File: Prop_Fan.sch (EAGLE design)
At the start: 120 parts, among them J1 1546215-2, J2 1546215-2, J3 1546215-2, J4 1546215-2, SW2 EVQ-Q2203W, SW3 EVQ-Q2203W, SW4 EVQ-Q2203W, U1 P8X32A-Q44, U10 MAX31855KASA+, U11 MAX31855KASA+, U12 MF-DSC-SOT233-BSS138, U13 MF-DSC-SOT233-BSS138, U14 CD74HC595M96, U16 CD74HC165M96, U17 MF-DSC-SOT233-BSS138, U18 MF-DSC-SOT233-BSS138, U19 MF-DSC-SOT233-BSS138, U2 MF-DSC-SOT233-BSS138, U3 MF-DSC-SOT233-BSS138, U4 MAX31855KASA+, U5 LM22678TJ-5.0/NOPB, U6 ADP3338AKCZ-3.3-RL, U7 CAT24C512WI-GT3, U8 MF-DSC-SOT233-BSS138, U9 MAX31855KASA+, X1 ABMM-6.000MHZ-B2-T

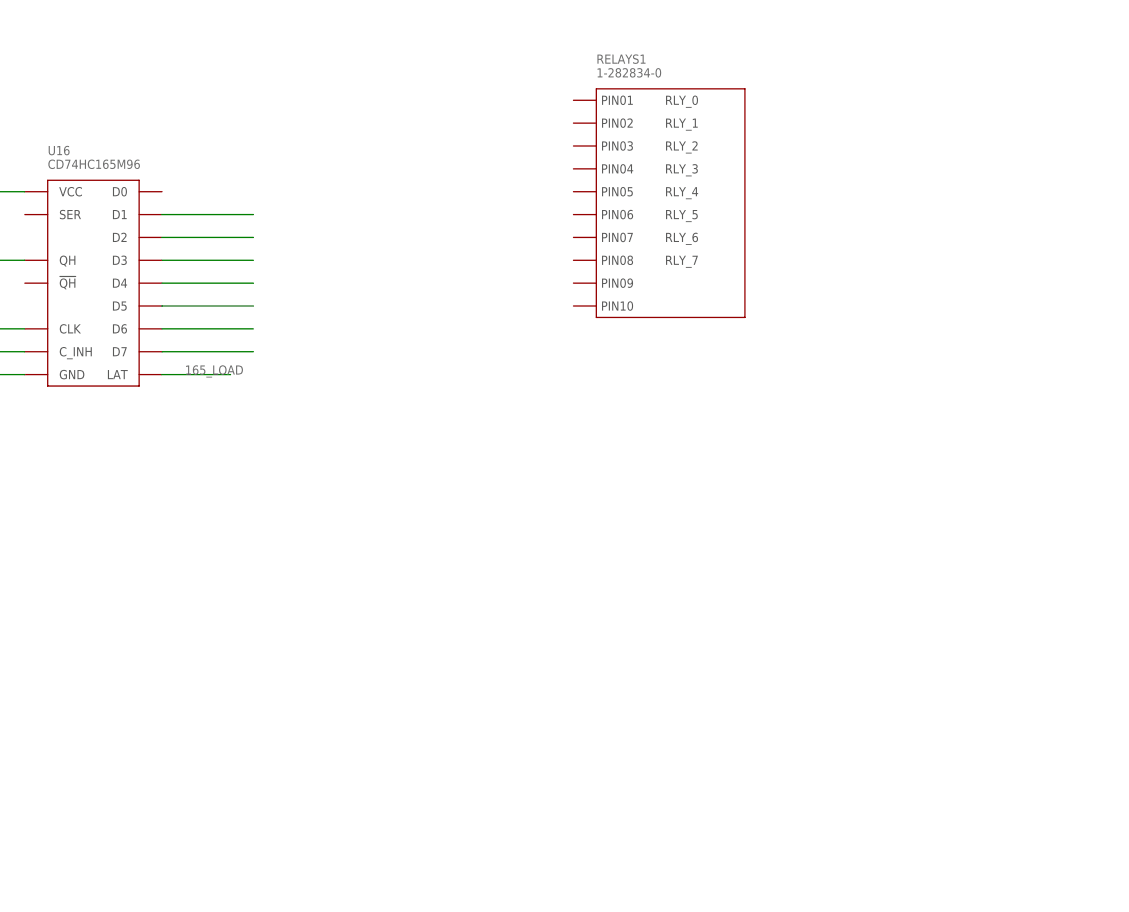
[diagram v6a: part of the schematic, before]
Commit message: Working on Switch inputs. Voltage Dividers!
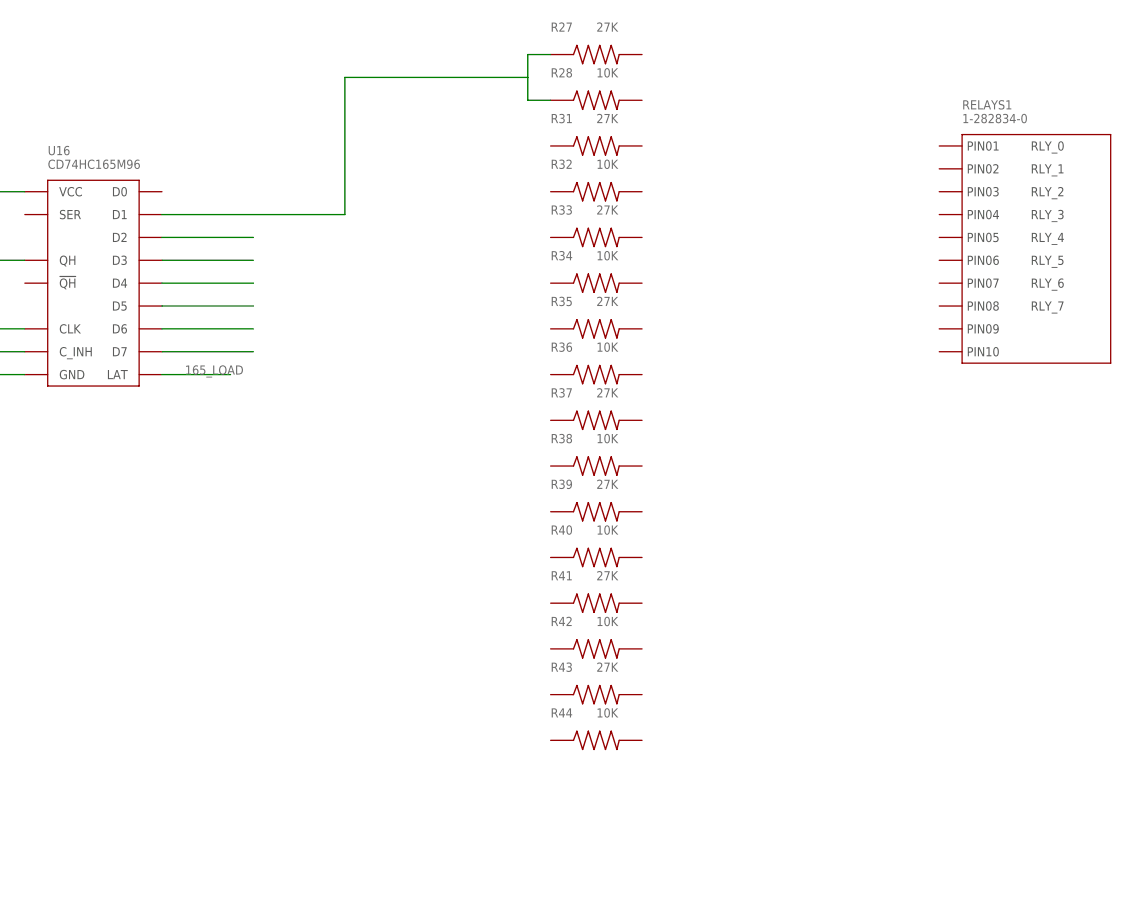
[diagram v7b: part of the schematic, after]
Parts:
- added R27, R31, R33, R35, R37, R39, R41, R43: 27K, MF_Passives:RESISTOR_0603
- added R28, R32, R34, R36, R38, R40, R42, R44: 10K, MF_Passives:RESISTOR_0603
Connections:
- net IN_OPTO_1: now also R27.P$1, R28.P$1
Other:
- moved on the sheet: RELAYS1
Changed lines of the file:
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@@
 <attribute name="LABEL08" value="RLY_7"/>
 </part>
+<part name="R27" library="MF_Passives" deviceset="RESISTOR" device="_0603" value="27K"/>
+<part name="R28" library="MF_Passives" deviceset="RESISTOR" device="_0603" value="10K"/>
+<part name="R31" library="MF_Passives" deviceset="RESISTOR" device="_0603" value="27K"/>
+<part name="R32" library="MF_Passives" deviceset="RESISTOR" device="_0603" value="10K"/>
+<part name="R33" library="MF_Passives" deviceset="RESISTOR" device="_0603" value="27K"/>
+<part name="R34" library="MF_Passives" deviceset="RESISTOR" device="_0603" value="10K"/>
+<part name="R35" library="MF_Passives" deviceset="RESISTOR" device="_0603" value="27K"/>
+<part name="R36" library="MF_Passives" deviceset="RESISTOR" device="_0603" value="10K"/>
+<part name="R37" library="MF_Passives" deviceset="RESISTOR" device="_0603" value="27K"/>
+<part name="R38" library="MF_Passives" deviceset="RESISTOR" device="_0603" value="10K"/>
+<part name="R39" library="MF_Passives" deviceset="RESISTOR" device="_0603" value="27K"/>
+<part name="R40" library="MF_Passives" deviceset="RESISTOR" device="_0603" value="10K"/>
+<part name="R41" library="MF_Passives" deviceset="RESISTOR" device="_0603" value="27K"/>
+<part name="R42" library="MF_Passives" deviceset="RESISTOR" device="_0603" value="10K"/>
+<part name="R43" library="MF_Passives" deviceset="RESISTOR" device="_0603" value="27K"/>
+<part name="R44" library="MF_Passives" deviceset="RESISTOR" device="_0603" value="10K"/>
 </parts>
 <sheets>
@@
 <instance part="U$4" gate="G$1" x="436.88" y="-22.86"/>
 <instance part="RELAYS" gate="G$1" x="472.44" y="170.18"/>
-<instance part="RELAYS1" gate="G$1" x="579.12" y="170.18"/>
+<instance part="RELAYS1" gate="G$1" x="619.76" y="165.1"/>
+<instance part="R27" gate="G$1" x="579.12" y="175.26"/>
+<instance part="R28" gate="G$1" x="579.12" y="170.18"/>
+<instance part="R31" gate="G$1" x="579.12" y="165.1"/>
+<instance part="R32" gate="G$1" x="579.12" y="160.02"/>
+<instance part="R33" gate="G$1" x="579.12" y="154.94"/>
+<instance part="R34" gate="G$1" x="579.12" y="149.86"/>
+<instance part="R35" gate="G$1" x="579.12" y="144.78"/>
+<instance part="R36" gate="G$1" x="579.12" y="139.7"/>
+<instance part="R37" gate="G$1" x="579.12" y="134.62"/>
+<instance part="R38" gate="G$1" x="579.12" y="129.54"/>
+<instance part="R39" gate="G$1" x="579.12" y="124.46"/>
+<instance part="R40" gate="G$1" x="579.12" y="119.38"/>
+<instance part="R41" gate="G$1" x="579.12" y="114.3"/>
+<instance part="R42" gate="G$1" x="579.12" y="109.22"/>
+<instance part="R43" gate="G$1" x="579.12" y="104.14"/>
+<instance part="R44" gate="G$1" x="579.12" y="99.06"/>
 </instances>
 <busses>
@@
 <segment>
 <pinref part="U16" gate="G$1" pin="D1"/>
-<wire x1="530.86" y1="157.48" x2="541.02" y2="157.48" width="0.1524" layer="91"/>
-</segment>
-</net>
+<pinref part="R27" gate="G$1" pin="P$1"/>
+<wire x1="574.04" y1="175.26" x2="571.5" y2="175.26" width="0.1524" layer="91"/>
+<wire x1="571.5" y1="175.26" x2="571.5" y2="172.72" width="0.1524" layer="91"/>
+<pinref part="R28" gate="G$1" pin="P$1"/>
+<wire x1="571.5" y1="172.72" x2="571.5" y2="170.18" width="0.1524" layer="91"/>
+<wire x1="571.5" y1="170.18" x2="574.04" y2="170.18" width="0.1524" layer="91"/>
+<wire x1="571.5" y1="172.72" x2="551.18" y2="172.72" width="0.1524" layer="91"/>
+<wire x1="551.18" y1="172.72" x2="551.18" y2="157.48" width="0.1524" layer="91"/>
+<wire x1="551.18" y1="157.48" x2="530.86" y2="157.48" width="0.1524" layer="91"/>
+</segment>
+</net>
